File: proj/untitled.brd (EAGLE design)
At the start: 64 parts, among them J1 SPKRAST_01532MR, J2 MICCMA-4544PF-W, J3 ADAFRUIT_OLED_13, U1 SIM5300EA, U10 3.3V 600mA, U2 MIC29302TO-263-5, U3 MCP23008QFN, U4 MCP23008QFN, U5 MCP23008QFN, U6 TXB0108, U7 SN74LVC1G125SOT23-5, U8 USIM_CONN, U9 ESDA6V1-5W6

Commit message: Completed mobile phone (untitled) schematic Started routing mobile phone board
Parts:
- added C25, C26, C30, C31, C42: 10uF, dooba:0805
- added C27, C28, C29, C32, C35, C36, C37, C38, C39, C45: 100nF, dooba:0805
- added C33, C34: 27pF, dooba:0805
- added C40: 470pF, dooba:0805
- added C41: 4.7nF, dooba:0805
- added C43, C44: 3.3uF, dooba:0805
- added C46, C47: 3.3nF, dooba:0805
- added C48, C51, C52, C53: 1uF, dooba:0805
- added C49, C50: 100uF, dooba:1210
- added J4: DM3D-SFDM, dooba:DM3D-SF
- added J5: SJ1-3523N, dooba:SJ1-352XN
- added J6: CONUFL001, dooba:CONUFL001
- added L1: 4.7uH, dooba:2520
- added R10, R14, R20: 10k, dooba:0805
- added R11: 1M, dooba:0805
- added R12, R13: 4.7R, dooba:0805
- added R15: 1k, dooba:0805
- added R16, R17: 560R, dooba:0805
- added R18, R19: 270k, dooba:0805
- added R22: 100k, dooba:0805
- added S1: SWITCH_SPDT, dooba:JS102011
- added U11: MCP1642B, dooba:MSOP8
- added U12: STA013LQFP44, dooba:QFP44
- added U13: CS4334, dooba:SO8
- added U14: LM4811PDSO-10, dooba:PDSO-10
- added X2: 14.7456MHz, dooba:XTAL_3225
- moved U8 427.1 mm to (59.7, 124.5), turned to 90 degrees
- moved C6 389.7 mm to (25.1, 113.5), flipped to the bottom, turned to 180 degrees
- moved C5 383.0 mm to (24.4, 111.0), flipped to the bottom, turned to 180 degrees
- moved R6 382.5 mm to (21.8, 113.5), flipped to the bottom
- moved R5 379.3 mm to (27.9, 109.7), flipped to the bottom, turned to 270 degrees
- moved U6 375.2 mm to (54.6, 121.9), flipped to the bottom, turned to 270 degrees
- moved R4 374.1 mm to (27.9, 106.4), flipped to the bottom, turned to 270 degrees
- moved C3 370.8 mm to (18.5, 113.5), flipped to the bottom
- moved C4 370.5 mm to (19.3, 111.0), flipped to the bottom
- moved R3 362.7 mm to (14.7, 109.0), flipped to the bottom, turned to 180 degrees
- moved U7 356.9 mm to (14.7, 106.4), flipped to the bottom, turned to 270 degrees
- moved U2 154.6 mm to (21.8, 99.6), flipped to the bottom, turned to 180 degrees
- moved U1 151.1 mm to (47.0, 100.3), flipped to the bottom
- moved N1 148.7 mm to (16.5, 127.0), flipped to the bottom
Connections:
- new net !STA013_RST: N1.25, R14.1, U12.25
- new net 5.0V: C23.2, C26.2, C3.1, C30.1, C4.1, C42.2, C45.1, J3.VIN, N1.16, N1.2, U10.1, U10.3, U11.4, U13.P$7, U2.P$2, U7.5
- new net AMP_SHUTDOWN: N1.30, R22.1, U14.7
- new net AMP_VOL_CLK: N1.29, U14.4
- new net AMP_VOL_UPDN: N1.28, U14.6
- new net AOUT_L: C46.1, C52.1, R17.2
- new net AOUT_R: C47.2, C53.1, R16.2
- new net I2C_SCL: J3.CLK, N1.23, R10.1, U12.32, U3.19, U4.19, U5.19
- new net I2C_SDA: J3.DATA, N1.24, R20.1, U12.31, U3.20, U4.20, U5.20
- new net MICROSD_CS: J4.DAT3/CS, N1.6
- new net N$35: C34.2, R11.1, U12.15, X2.1
- new net N$40: C33.2, R11.2, U12.13, X2.3
- new net N$41: L1.2, U11.5
- new net N$42: C39.1, R13.2, U12.10
- new net N$45: C39.2, R12.1, U12.11
- new net N$46: C41.2, R15.2
- new net N$49: C40.2, R15.1, U12.12
- new net N$50: C43.2, R18.1, U13.P$8
- new net N$51: C44.2, R19.2, U13.P$5
- new net N$52: C44.1, R16.1
- new net N$53: C43.1, R17.1
- new net N$54: C49.2, U14.1
- new net N$55: C50.2, U14.9
- new net N$56: C51.2, U14.3
- new net N$57: C50.1, J5.3
- new net N$58: C52.2, U14.2
- new net N$59: C53.2, U14.8
- new net N$60: C49.1, J5.2
- new net N$61: J6.P$3, U1.P$60
- new net SPI_MISO: J4.DAT0/DO, N1.32
- new net SPI_MOSI: J4.CMD/DI, N1.31, U12.34
- new net SPI_SCK: J4.CLK/SCK, N1.33, U12.36
- new net STA013_BIT_EN: N1.27, U12.38
- new net STA013_DREQ: N1.26, U12.27
- new net STA013_LRCKT: U12.2, U13.P$3
- new net STA013_OCLK: U12.3, U13.P$4
- new net STA013_SCKT: U12.44, U13.P$2
- new net STA013_SDO: U12.42, U13.P$1
- new net VBAT: S1.2
- net 3.3V: now also C27.2, C28.2, C29.1, C31.1, C32.1, C35.2, C36.2, C37.2, C38.2, C48.2, J4.VDD, R10.2, R13.1, R14.2, R20.2, R22.2, U12.21, U12.22, U12.29, U12.40, U12.6, U12.8, U14.10, U3.1, U3.18, U3.4, U4.1, U4.18, U4.3, U4.4, U5.1, U5.18, U5.2, U5.4
- net GND: now also B1.2, B10.2, B11.2, B12.2, B13.5, B13.GND1, B13.GND2, B14.1, B15.2, B16.1, B17.2, B2.2, B3.2, B4.2, B5.2, B6.2, B7.2, B8.2, B9.2, C25.2, C26.1, C27.1, C28.1, C29.2, C30.2, C31.2, C32.2, C33.1, C34.1, C35.1, C36.1, C37.1, C38.1, C40.1, C41.1, C42.1, C45.2, C46.2, C47.1, C48.1, C51.1, J3.GND, J4.GND1, J4.GND2, J4.GND3, J4.GND4, J4.VSS, J5.1, J6.P$1, J6.P$2, N1.1, N1.15, N1.35, R12.2, R18.2, R19.1, U11.6, U11.7, U12.19, U12.24, U12.26, U12.30, U12.5, U12.7, U13.P$6, U14.5, U3.17, U3.2, U3.3, U3.PAD, U4.17, U4.2, U4.PAD, U5.17, U5.3, U5.PAD, X2.2, X2.4
- net GSM_PWR_EN: now also N1.10
- net GSM_PWR_KEY: now also N1.9
- net GSM_RING: now also N1.7
- net GSM_RXD: now also N1.18
- net GSM_STATUS: now also N1.8
- net GSM_TXD: now also N1.17
- net VIN: now also C25.1, L1.1, S1.3, U11.1, U11.8; no longer C23.2, C3.1, C4.1, U10.1, U10.3, U2.P$2, U7.5

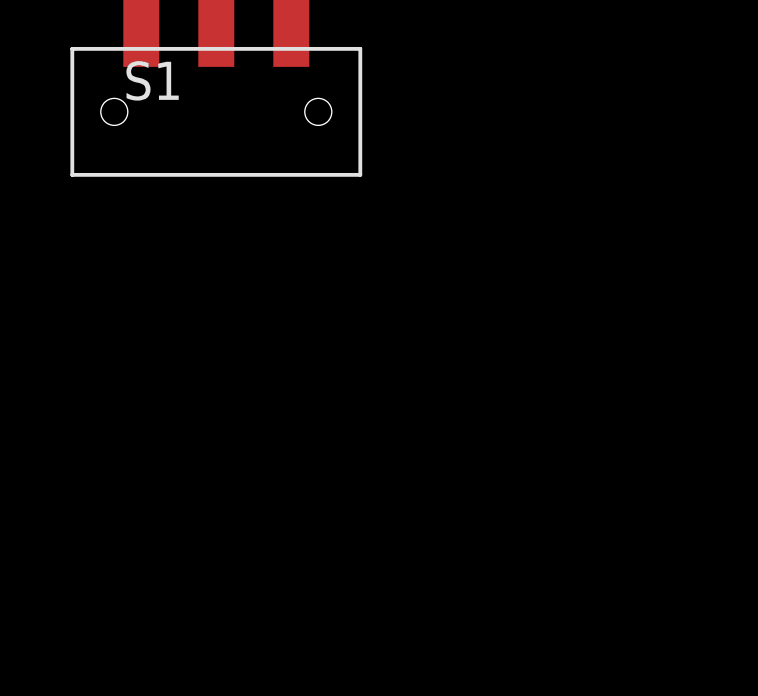
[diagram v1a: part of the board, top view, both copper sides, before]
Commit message: Added Z3OC Vibration Motor to Eagle Library Added Vibrator to mobile phone schematic
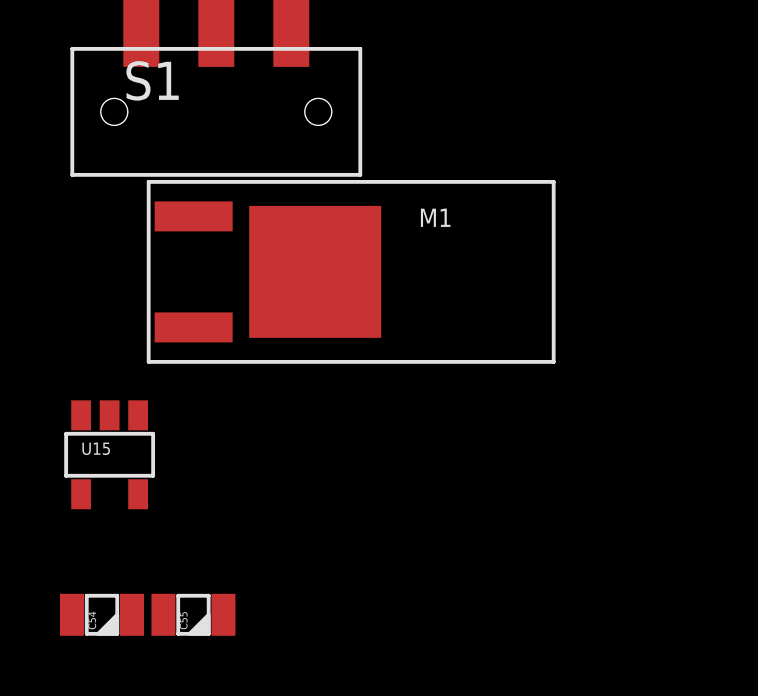
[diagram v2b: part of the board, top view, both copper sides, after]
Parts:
- added C54, C55: 1uF, dooba:0805
- added M1: Z3OC_VIB_MOTOR, dooba:Z3OC_VIB_MOTOR
- added U15: 2.7V 200mA, dooba:SOT23-5
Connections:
- new net 2.7V: C55.2, M1.2, U15.5
- new net VIBRATOR_EN: U15.3
- net 5.0V: now also C54.2, U15.1
- net GND: now also C54.1, C55.1, M1.1, U15.2
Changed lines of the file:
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@@
 <element name="S1" library="dooba" package="JS102011" value="SWITCH_SPDT" x="-168.91" y="-538.48"/>
 <element name="J6" library="dooba" package="CONUFL001" value="CONUFL001" x="46.99" y="118.11" rot="MR0"/>
+<element name="M1" library="dooba" package="Z3OC_VIB_MOTOR" value="Z3OC_VIB_MOTOR" x="-169.164" y="-543.814"/>
+<element name="U15" library="dooba" package="SOT23-5" value="2.7V 200mA" x="-172.466" y="-549.91"/>
+<element name="C54" library="dooba" package="0805" value="1uF" x="-172.72" y="-555.244"/>
+<element name="C55" library="dooba" package="0805" value="1uF" x="-169.672" y="-555.244"/>
 </elements>
 <signals>
@@
 <contactref element="J6" pad="P$1"/>
 <contactref element="J6" pad="P$2"/>
+<contactref element="U15" pad="2"/>
+<contactref element="C54" pad="1"/>
+<contactref element="C55" pad="1"/>
+<contactref element="M1" pad="1"/>
 <wire x1="-73.85" y1="-170.18" x2="-76.01" y2="-179.07" width="0" layer="19" extent="1-1"/>
 <wire x1="-71.12" y1="-160.36" x2="-73.85" y2="-170.18" width="0" layer="19" extent="1-1"/>
@@
 <wire x1="-156.48" y1="-513.08" x2="-154.67" y2="-508" width="0" layer="19" extent="1-1"/>
 <wire x1="-172.43" y1="-519.16" x2="-173.72" y2="-513.08" width="0" layer="19" extent="1-1"/>
+<wire x1="-169.664" y1="-541.964" x2="-172.43" y2="-519.16" width="0" layer="19" extent="1-1"/>
+<wire x1="-172.466" y1="-548.595" x2="-169.664" y2="-541.964" width="0" layer="19" extent="1-1"/>
+<wire x1="-173.72" y1="-555.244" x2="-172.466" y2="-548.595" width="0" layer="19" extent="1-1"/>
+<wire x1="-170.672" y1="-555.244" x2="-173.72" y2="-555.244" width="0" layer="19" extent="1-1"/>
 <wire x1="43.99" y1="87.33" x2="-15.05" y2="-63.5" width="0" layer="19" extent="1-16"/>
 <wire x1="54.99" y1="87.33" x2="43.99" y2="87.33" width="0" layer="19" extent="16-16"/>
@@
 <wire x1="25.984" y1="110.998" x2="27.94" y2="105.426" width="0" layer="19" extent="16-16"/>
 <wire x1="26.146" y1="113.538" x2="25.984" y2="110.998" width="0" layer="19" extent="16-16"/>
-<wire x1="21.844" y1="106.368" x2="25.984" y2="110.998" width="0" layer="19" extent="16-16"/>
-<wire x1="13.417" y1="107.376" x2="21.844" y2="106.368" width="0" layer="19" extent="16-16"/>
+<wire x1="20.844" y1="113.538" x2="26.146" y2="113.538" width="0" layer="19" extent="16-16"/>
+<wire x1="17.542" y1="113.538" x2="20.844" y2="113.538" width="0" layer="19" extent="16-16"/>
+<wire x1="17.704" y1="110.998" x2="17.542" y2="113.538" width="0" layer="19" extent="16-16"/>
+<wire x1="15.732" y1="108.966" x2="17.704" y2="110.998" width="0" layer="19" extent="16-16"/>
+<wire x1="13.417" y1="107.376" x2="15.732" y2="108.966" width="0" layer="19" extent="16-16"/>
 <wire x1="13.417" y1="105.476" x2="13.417" y2="107.376" width="0" layer="19" extent="16-16"/>
-<wire x1="17.704" y1="110.998" x2="13.417" y2="107.376" width="0" layer="19" extent="16-16"/>
-<wire x1="17.542" y1="113.538" x2="17.704" y2="110.998" width="0" layer="19" extent="16-16"/>
+<wire x1="21.844" y1="106.368" x2="27.94" y2="105.426" width="0" layer="19" extent="16-16"/>
 <wire x1="21.844" y1="97.263" x2="21.844" y2="106.368" width="0" layer="19" extent="16-16"/>
-<wire x1="15.732" y1="108.966" x2="26.146" y2="113.538" width="0" layer="19" extent="16-16"/>
-<wire x1="38.1" y1="121.92" x2="15.732" y2="108.966" width="0" layer="19" extent="16-16"/>
-<wire x1="20.844" y1="113.538" x2="38.1" y2="121.92" width="0" layer="19" extent="16-16"/>
-<wire x1="45.49" y1="118.11" x2="20.844" y2="113.538" width="0" layer="19" extent="16-16"/>
-<wire x1="48.49" y1="118.11" x2="45.49" y2="118.11" width="0" layer="19" extent="16-16"/>
-<wire x1="48.49" y1="117.26" x2="48.49" y2="118.11" width="0" layer="19" extent="1-16"/>
-<wire x1="51.685" y1="118.995" x2="48.49" y2="118.11" width="0" layer="19" extent="16-16"/>
-<wire x1="48.99" y1="113.33" x2="48.49" y2="117.26" width="0" layer="19" extent="1-16"/>
+<wire x1="40.99" y1="113.33" x2="33.99" y2="103.33" width="0" layer="19" extent="16-16"/>
+<wire x1="44.99" y1="113.33" x2="40.99" y2="113.33" width="0" layer="19" extent="16-16"/>
+<wire x1="45.99" y1="113.33" x2="44.99" y2="113.33" width="0" layer="19" extent="16-16"/>
+<wire x1="47.99" y1="113.33" x2="45.99" y2="113.33" width="0" layer="19" extent="16-16"/>
+<wire x1="48.99" y1="113.33" x2="47.99" y2="113.33" width="0" layer="19" extent="16-16"/>
 <wire x1="49.99" y1="113.33" x2="48.99" y2="113.33" width="0" layer="19" extent="16-16"/>
 <wire x1="50.99" y1="113.33" x2="49.99" y2="113.33" width="0" layer="19" extent="16-16"/>
 <wire x1="51.99" y1="113.33" x2="50.99" y2="113.33" width="0" layer="19" extent="16-16"/>
-<wire x1="47.99" y1="113.33" x2="48.99" y2="113.33" width="0" layer="19" extent="16-16"/>
-<wire x1="45.99" y1="113.33" x2="47.99" y2="113.33" width="0" layer="19" extent="16-16"/>
-<wire x1="44.99" y1="113.33" x2="45.99" y2="113.33" width="0" layer="19" extent="16-16"/>
-<wire x1="40.99" y1="113.33" x2="44.99" y2="113.33" width="0" layer="19" extent="16-16"/>
+<wire x1="48.49" y1="117.26" x2="47.99" y2="113.33" width="0" layer="19" extent="1-16"/>
+<wire x1="48.49" y1="118.11" x2="48.49" y2="117.26" width="0" layer="19" extent="1-16"/>
+<wire x1="45.49" y1="118.11" x2="48.49" y2="118.11" width="0" layer="19" extent="16-16"/>
+<wire x1="51.685" y1="118.995" x2="48.49" y2="118.11" width="0" layer="19" extent="16-16"/>
 <wire x1="59.69" y1="121.01" x2="51.685" y2="118.995" width="0" layer="19" extent="1-16"/>
+<wire x1="38.1" y1="121.92" x2="45.49" y2="118.11" width="0" layer="19" extent="16-16"/>
 <wire x1="59.99" y1="107.33" x2="51.99" y2="113.33" width="0" layer="19" extent="16-16"/>
 <wire x1="35.56" y1="133.35" x2="38.1" y2="121.92" width="0" layer="19" extent="1-1"/>
@@
 <contactref element="C23" pad="2"/>
 <contactref element="U10" pad="3"/>
+<contactref element="U15" pad="1"/>
+<contactref element="C54" pad="2"/>
 <wire x1="-139.38" y1="-363.175" x2="-138.7" y2="-368.3" width="0" layer="19" extent="1-1"/>
 <wire x1="-137.48" y1="-363.175" x2="-139.38" y2="-363.175" width="0" layer="19" extent="1-1"/>
@@
 <wire x1="-128" y1="-508" x2="-126.365" y2="-492.76" width="0" layer="19" extent="1-1"/>
 <wire x1="-137.43" y1="-508" x2="-128" y2="-508" width="0" layer="19" extent="1-1"/>
+<wire x1="-171.516" y1="-548.595" x2="-137.43" y2="-508" width="0" layer="19" extent="1-1"/>
+<wire x1="-171.72" y1="-555.244" x2="-171.516" y2="-548.595" width="0" layer="19" extent="1-1"/>
 <wire x1="16.047" y1="105.476" x2="-116.84" y2="-330.2" width="0" layer="19" extent="16-16"/>
 <wire x1="20.144" y1="106.368" x2="16.047" y2="105.476" width="0" layer="19" extent="16-16"/>
@@
 <wire x1="46.99" y1="113.33" x2="46.99" y2="116.61" width="0" layer="19" extent="16-16"/>
 </signal>
+<signal name="2.7V">
+<contactref element="U15" pad="5"/>
+<contactref element="C55" pad="2"/>
+<contactref element="M1" pad="2"/>
+<wire x1="-168.672" y1="-555.244" x2="-171.516" y2="-551.225" width="0" layer="19" extent="1-1"/>
+<wire x1="-169.664" y1="-545.664" x2="-171.516" y2="-551.225" width="0" layer="19" extent="1-1"/>
+</signal>
+<signal name="VIBRATOR_EN">
+<contactref element="U15" pad="3"/>
+</signal>
 </signals>

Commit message: Further routed mobile phone board
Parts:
- added BAT[+-]: PIN_2, dooba:PIN_2
- added R23: 10k, dooba:0805
- added U16: SN74LVC1G125SOT23-5, dooba:SOT23-5
- moved S1 633.2 mm to (4.06, 70.6), turned to 270 degrees
- moved C54 626.4 mm to (50.8, 30.0), flipped to the bottom, turned to 90 degrees
- moved C55 625.9 mm to (54.4, 29.2), flipped to the bottom, turned to 180 degrees
- moved U15 624.1 mm to (53.8, 31.8), flipped to the bottom, turned to 270 degrees
- moved M1 611.7 mm to (52.8, 26.2), flipped to the bottom, turned to 270 degrees
- moved R20 590.8 mm to (22.9, 29.2), flipped to the bottom, turned to 270 degrees
- moved R10 585.5 mm to (21.1, 29.2), flipped to the bottom, turned to 270 degrees
- moved C34 582.3 mm to (13.7, 45.0), flipped to the bottom, turned to 90 degrees
- moved C33 581.6 mm to (7.62, 45.0), flipped to the bottom, turned to 270 degrees
- moved R11 580.3 mm to (10.7, 41.1), flipped to the bottom
- moved C37 575.9 mm to (16.0, 41.1), flipped to the bottom, turned to 180 degrees
- moved R14 575.6 mm to (21.1, 36.6), flipped to the bottom, turned to 90 degrees
- moved R12 575.3 mm to (3.94, 39.1), flipped to the bottom
- moved R15 575.2 mm to (5.84, 41.7), flipped to the bottom, turned to 90 degrees
- moved X2 573.1 mm to (10.7, 44.5), flipped to the bottom, turned to 270 degrees
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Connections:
- new net N$62: U15.3, U16.4
- net 5.0V: now also U16.5
- net GND: now also BAT[+-].2, R23.2, U16.1, U16.3
- net GSM_PWR_KEY: now also N1.8; no longer N1.9
- net GSM_RING: now also N1.9; no longer N1.7
- net GSM_STATUS: now also N1.7; no longer N1.8
- net N$18: now also B4.1; no longer B7.1
- net N$19: now also B7.1; no longer B4.1
- net VBAT: now also BAT[+-].1
- net VIBRATOR_EN: now also N1.14, R23.1, U16.2; no longer U15.3
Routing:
- net I2C_SCL: track 0.00 -> 149.0 mm, vias 0 -> 4
- net I2C_SDA: track 0.00 -> 137.5 mm, vias 0 -> 3
- net N$47: track 0.00 -> 91.6 mm, vias 0 -> 4
- net N$48: track 0.00 -> 91.4 mm, vias 0 -> 4
- net SPI_MOSI: track 0.00 -> 69.2 mm, vias 0 -> 1
- net AMP_VOL_UPDN: track 0.00 -> 64.0 mm, vias 0 -> 2
- net SPI_SCK: track 0.00 -> 62.9 mm, vias 0 -> 1
- net AMP_SHUTDOWN: track 0.00 -> 62.4 mm
- net AMP_VOL_CLK: track 0.00 -> 57.9 mm, vias 0 -> 2
- net GSM_PWR_EN: track 0.00 -> 54.7 mm, vias 0 -> 2
- net MICROSD_CS: track 0.00 -> 51.3 mm, vias 0 -> 1
- net GSM_RXD: track 0.00 -> 45.2 mm
- net 3.3V: track 0.00 -> 42.5 mm, vias 0 -> 2
- net GSM_TXD: track 0.00 -> 39.6 mm
- net VIBRATOR_EN: track 0.00 -> 38.8 mm, vias 0 -> 1
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- added copper zone on layer 1, net GND
- added copper zone on layer 16, net GND
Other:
- board outline added: 58.4 x 122.7 mm

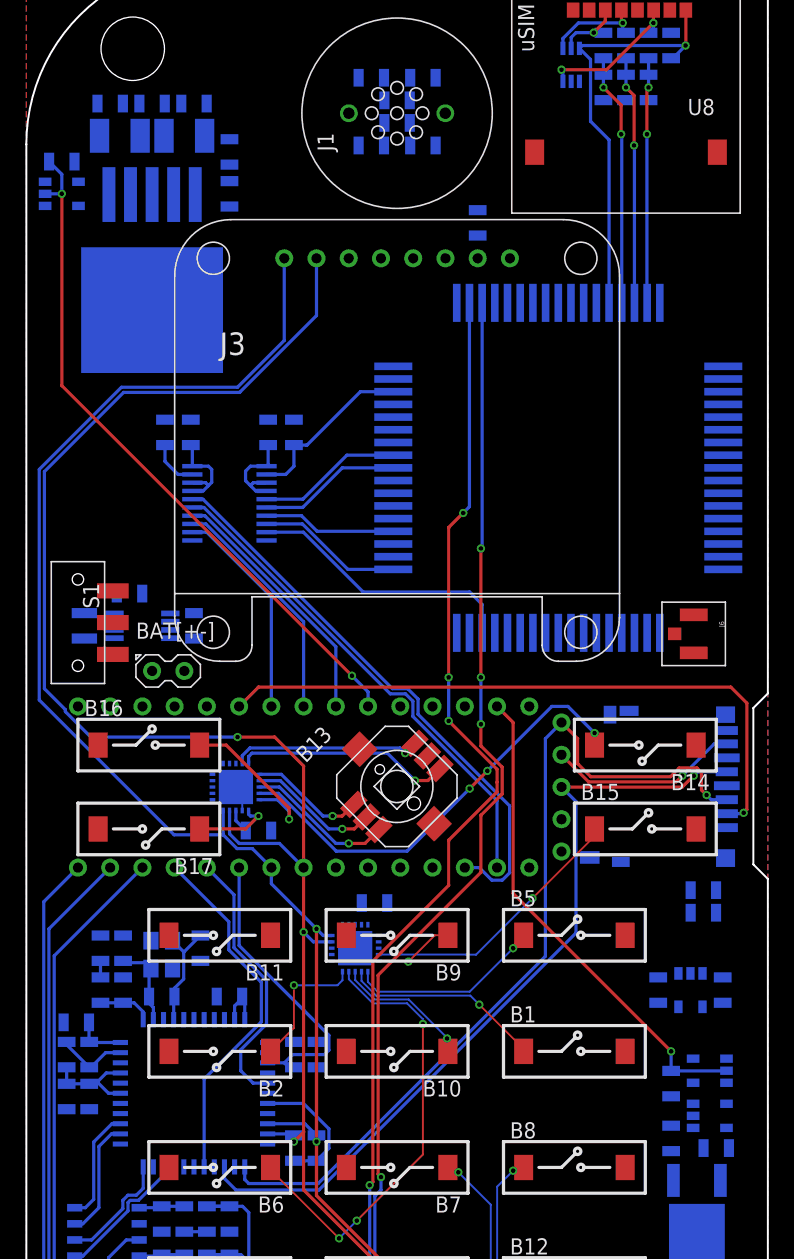
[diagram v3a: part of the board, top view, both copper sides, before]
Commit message: Further routed mobile phone board
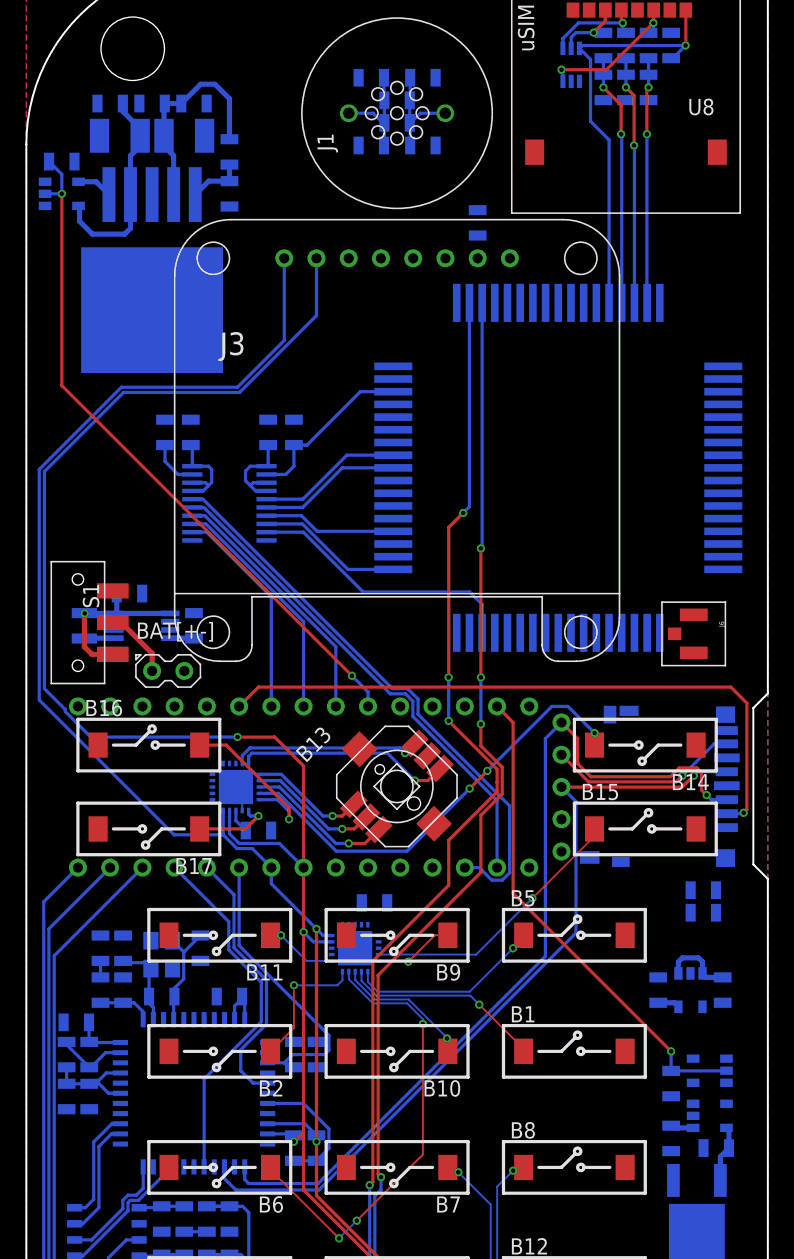
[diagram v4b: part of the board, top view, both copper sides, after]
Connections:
- net 5.0V: no longer N1.2
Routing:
- net 5.0V: track 5.96 -> 31.9 mm
- net 3.8V: track 0.00 -> 16.9 mm
- net VIN: track 0.00 -> 13.5 mm, vias 0 -> 1
- net N$44: track 0.00 -> 8.53 mm
- net N$43: track 0.00 -> 8.46 mm
- net N$16: track 0.00 -> 5.65 mm, vias 0 -> 1
- net VBAT: track 0.00 -> 5.49 mm
- net 2.7V: track 0.00 -> 4.50 mm
- net N$29: track 0.00 -> 4.44 mm
- net N$28: track 0.00 -> 2.81 mm
- net N$41: track 0.00 -> 2.38 mm
- net 3.3V: track 42.5 -> 44.2 mm
